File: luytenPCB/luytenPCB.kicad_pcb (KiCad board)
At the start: 2 copper layers, 35 parts, among them IC1 DRV8212DRLR, IC2 DRV8212DRLR, J1 Battery, J10 START_M, J2 BDC1, J3 BDC2, J4 LINE_RF, J5 LINE_LF, J6 DIST_L, J7 DIST_LM, J8 DIST_R, J9 DIST_RM, SW1 SW_SPST, SW2 ProgSelect

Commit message: pcb production prototype done
finished schematic and layout
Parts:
- added F1: 15A, Fuse:Fuse_1206_3216Metric_Pad1.42x1.75mm_HandSolder, F.Cu at (89.3, 46.2)
- added H1: MountingHole, MountingHole:MountingHole_2.2mm_M2_ISO7380, F.Cu at (44.3, 33.0)
- added H2: MountingHole, MountingHole:MountingHole_2.2mm_M2_ISO7380, F.Cu at (120.3, 33.0)
- added H3: MountingHole, MountingHole:MountingHole_2.2mm_M2_ISO7380, F.Cu at (44.3, 57.0)
- added H4: MountingHole, MountingHole:MountingHole_2.2mm_M2_ISO7380, F.Cu at (120.3, 57.0)
- J1: footprint Connector_AMASS:AMASS_XT30PW-M_1x02_P2.50mm_Horizontal -> Connector_AMASS:AMASS_XT30U-M_1x02_P5.0mm_Vertical
- moved C4 74.9 mm to (55.1, 41.5)
- moved C5 74.9 mm to (55.1, 44.5)
- moved C6 74.9 mm to (55.1, 47.5)
- moved C3 44.8 mm to (85.3, 41.7), turned to 180 degrees
- moved C2 43.4 mm to (85.3, 44.7), turned to 180 degrees
- moved C1 42.7 mm to (85.3, 47.7), turned to 180 degrees
- moved IC2 37.6 mm to (93.0, 37.9)
- moved C7 36.6 mm to (96.5, 38.2), turned to 90 degrees
- moved D3 32.4 mm to (81.2, 54.3)
- moved D4 26.2 mm to (71.1, 54.3)
- moved R1 26.1 mm to (103.5, 53.8), turned to 90 degrees
- moved R3 23.4 mm to (85.7, 54.0), turned to 180 degrees
- moved J1 22.8 mm to (114.9, 36.4)
- moved D1 21.0 mm to (103.5, 48.9), turned to -90 degrees
- moved R2 20.8 mm to (100.3, 53.8), turned to 90 degrees
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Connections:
- A1 pad D11: MDC2_2 -> MDC2_1
- A1 pad D12: MDC2_1 -> MDC2_2
- A1 pad D2: MDC1_2 -> MDC1_1
- A1 pad D3: MDC1_1 -> MDC1_2
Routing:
- net Arduino3.3V: track 0.00 -> 157.4 mm, vias 0 -> 3
- net START_SIGNAL: track 0.00 -> 67.7 mm, vias 0 -> 2
- net PS3: track 0.00 -> 53.1 mm, vias 0 -> 2
- net Net-(IC2-OUT1): track 0.00 -> 47.8 mm, vias 0 -> 2
- net DIST_L_INT: track 0.00 -> 47.4 mm, vias 0 -> 1
- net ArduinoVIN: track 0.00 -> 47.4 mm, vias 0 -> 4
- net PS2: track 0.00 -> 46.2 mm, vias 0 -> 2
- net Net-(IC2-OUT2): track 0.00 -> 44.8 mm, vias 0 -> 2
- net GND: track 0.00 -> 44.3 mm, vias 0 -> 8
- net MDC2_2: track 0.00 -> 43.4 mm, vias 0 -> 2
- net MDC2_1: track 0.00 -> 39.9 mm, vias 0 -> 2
- net PS1: track 0.00 -> 39.0 mm, vias 0 -> 2
- net Net-(IC1-OUT2): track 0.00 -> 32.3 mm, vias 0 -> 2
- net DIST_LM_INT: track 0.00 -> 31.7 mm
- net Net-(J1-Pin_1): track 0.00 -> 28.4 mm, vias 0 -> 2
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- added copper zone on B.Cu, net GND
- added copper zone on F.Cu, net GND
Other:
- board outline added: 80.9 x 35.6 mm
- board text added: "LUYTEN"
- board text added: "Luyten_MiniSumo_v0 - Alex Peng '24"

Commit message: updates
--fixes to routing, updated screw terminal
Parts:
- added D7: GREEN, Capacitor_SMD:C_0603_1608Metric_Pad1.08x0.95mm_HandSolder, F.Cu at (73.9, 55.6)
- added J11: DIST_C, Connector_PinHeader_2.54mm:PinHeader_1x03_P2.54mm_Vertical, F.Cu at (72.4, 58.8)
- added R7: 100, Diode_SMD:D_0805_2012Metric_Pad1.15x1.40mm_HandSolder, F.Cu at (74.0, 53.6)
- J2, J3: footprint Connector_Phoenix_MSTB:PhoenixContact_MSTBA_2,5_2-G_1x02_P5.00mm_Horizontal -> Connector_PinHeader_2.54mm:PinHeader_1x02_P2.54mm_Vertical
- J4, J5, J6, J7, J8, J9: footprint Connector_Phoenix_MSTB:PhoenixContact_MSTBA_2,5_3-G_1x03_P5.00mm_Horizontal -> Connector_PinHeader_2.54mm:PinHeader_1x03_P2.54mm_Vertical
- moved D3 16.7 mm to (97.6, 57.3)
- moved R3 16.7 mm to (102.1, 57.0)
- moved J4 14.7 mm to (58.8, 31.0), turned to 90 degrees
- moved D4 11.5 mm to (82.5, 54.9)
- moved R4 11.5 mm to (87.4, 54.7)
- moved J9 7.05 mm to (61.5, 58.7), turned to 90 degrees
- moved J6 6.50 mm to (97.8, 60.1), turned to 90 degrees
- moved J3 5.62 mm to (50.2, 31.0), turned to 90 degrees
- moved J5 4.54 mm to (105.7, 31.4), turned to -90 degrees
- moved D6 3.96 mm to (54.7, 55.4), turned to 180 degrees
- moved R5 3.79 mm to (62.1, 53.6)
- moved J7 1.64 mm to (85.2, 59.8), turned to 90 degrees
- moved D5 1.51 mm to (61.9, 55.6), turned to 180 degrees
- moved R6 1.18 mm to (54.5, 53.4)
- moved J2 1.01 mm to (114.9, 30.7), turned to -90 degrees
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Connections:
- A1 pad A4: unconnected-(A1-A4/SDA-PadA4) -> MDC2_1
- A1 pad A5: unconnected-(A1-A5/SCL-PadA5) -> MDC2_2
- A1 pad A6: unconnected-(A1-PadA6) -> MDC1_1
- A1 pad A7: unconnected-(A1-PadA7) -> MDC1_2
- A1 pad D11: MDC2_1 -> unconnected-(A1-D11_MOSI-PadD11)
- A1 pad D12: MDC2_2 -> unconnected-(A1-D12_MISO-PadD12)
- A1 pad D2: MDC1_1 -> unconnected-(A1-PadD2)
- A1 pad D3: MDC1_2 -> unconnected-(A1-PadD3)
- A1 pad D9: unconnected-(A1-PadD9) -> DIST_C_INT
- J1 pad 1: Net-(J1-Pin_1) -> GND
- J1 pad 2: GND -> Net-(J1-Pin_2)
- SW1 pad 2: Net-(J1-Pin_1) -> Net-(J1-Pin_2)
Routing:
- net Arduino3.3V: track 157.4 -> 27.8 mm, vias 3 -> 0
- net Net-(IC2-OUT1): track 47.8 -> 0.00 mm, vias 2 -> 0
- net DIST_L_INT: track 47.4 -> 0.00 mm, vias 1 -> 0
- net Net-(IC2-OUT2): track 44.8 -> 0.00 mm, vias 2 -> 0
- net Net-(IC1-OUT2): track 32.3 -> 0.00 mm, vias 2 -> 0
- net DIST_LM_INT: track 31.7 -> 0.00 mm
- net Net-(J1-Pin_1): track 28.4 -> 0.00 mm, vias 2 -> 0
- net LF_INT: track 27.7 -> 0.00 mm
- net Net-(IC1-OUT1): track 25.6 -> 0.00 mm, vias 2 -> 0
- net Net-(J1-Pin_2): track 0.00 -> 23.8 mm, vias 0 -> 2
- net DIST_RM_INT: track 18.4 -> 0.00 mm
- net MDC2_2: track 43.4 -> 27.8 mm, vias 2 -> 0
- net RF_INT: track 14.3 -> 0.00 mm
- net DIST_R_INT: track 9.76 -> 0.00 mm
- net MDC2_1: track 39.9 -> 30.4 mm, vias 2 -> 0
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- removed copper zone on B.Cu, net GND
- removed copper zone on F.Cu, net GND

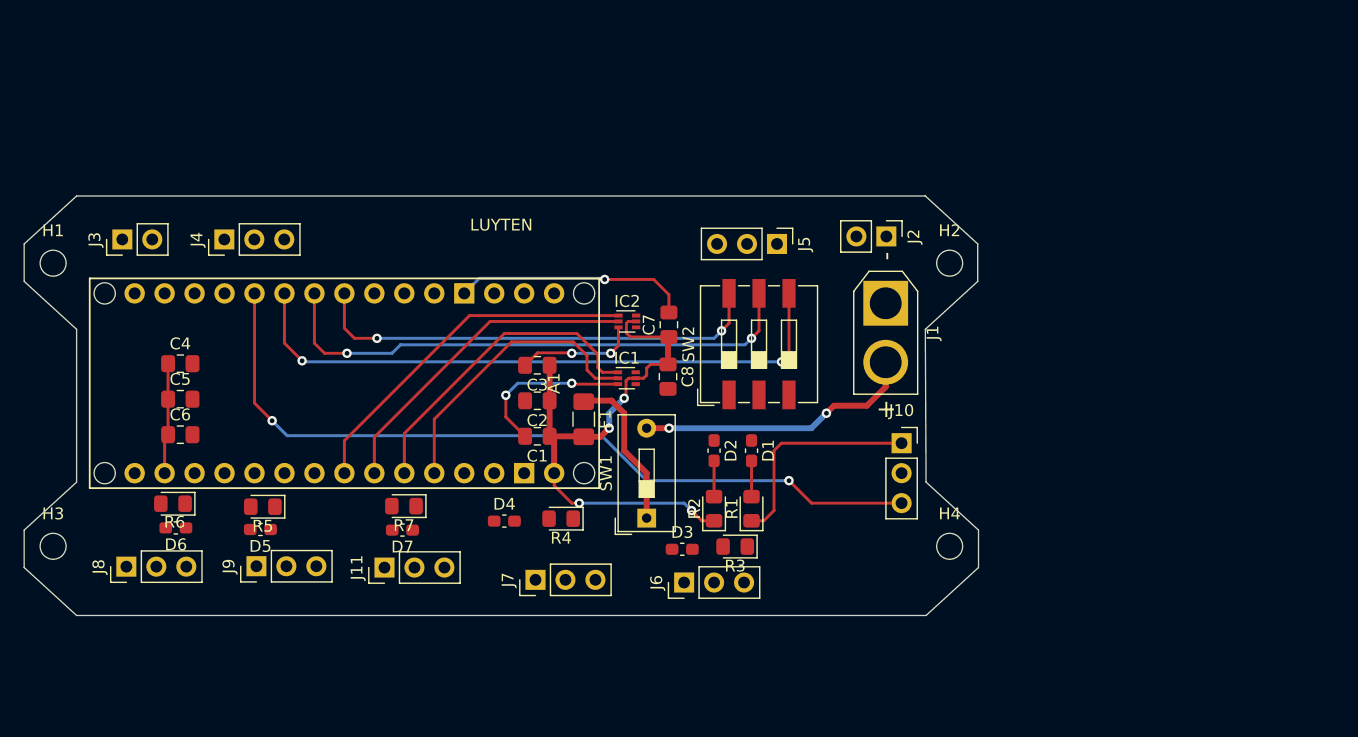
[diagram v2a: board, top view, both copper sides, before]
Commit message: luytenv2
forgot to update spst footprint :(
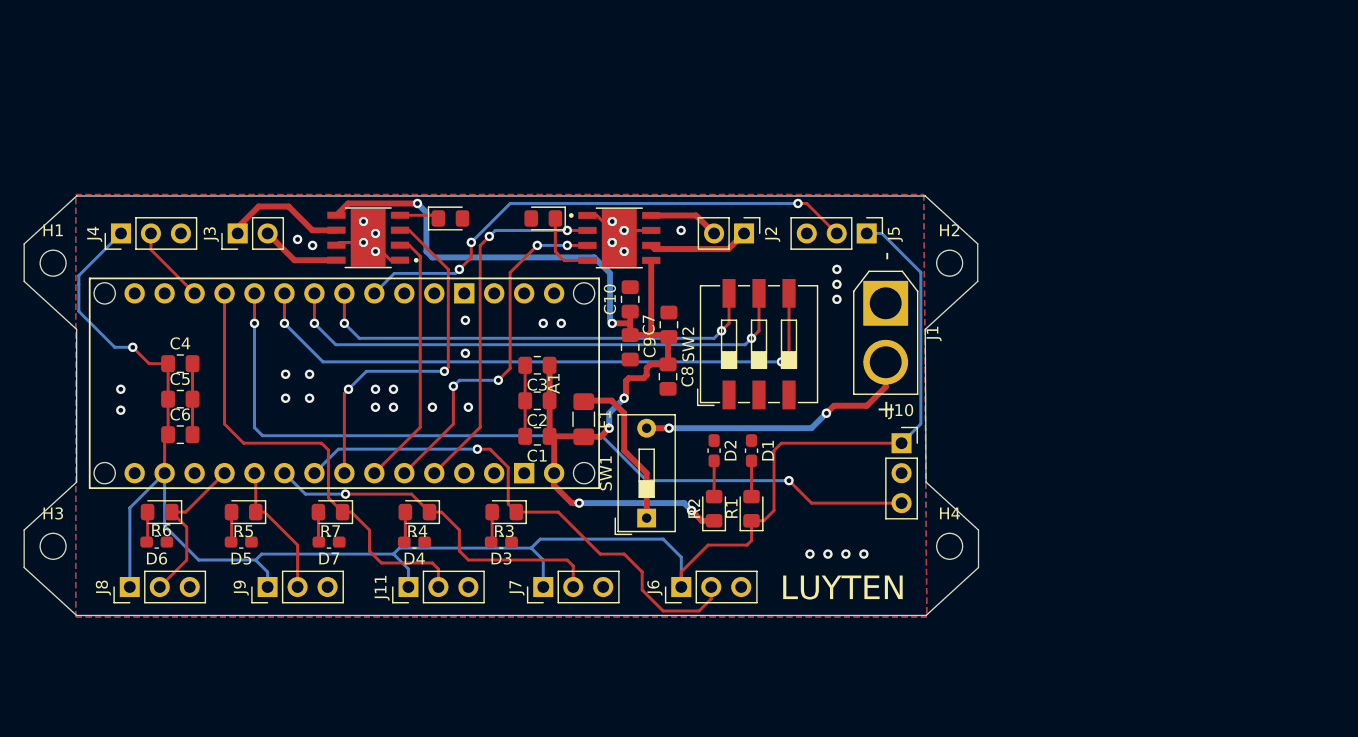
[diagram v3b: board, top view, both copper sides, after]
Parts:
- added C10: 47uF, Capacitor_SMD:C_0805_2012Metric_Pad1.18x1.45mm_HandSolder, F.Cu at (93.2, 36.1)
- added C9: 47uF, Capacitor_SMD:C_0805_2012Metric_Pad1.18x1.45mm_HandSolder, F.Cu at (93.2, 40.1)
- added R8: 30k, Diode_SMD:D_0805_2012Metric_Pad1.15x1.40mm_HandSolder, F.Cu at (85.9, 29.2)
- added R9: 30k, Diode_SMD:D_0805_2012Metric_Pad1.15x1.40mm_HandSolder, F.Cu at (78.0, 29.2)
- IC1, IC2: footprint Package_TO_SOT_SMD:SOT-563 -> DRV8871DDAR:VREG_LM5017MR_NOPB
- moved IC2 23.1 mm to (71.0, 30.8), turned to 180 degrees
- moved R3 19.8 mm to (82.5, 54.1)
- moved D3 15.3 mm to (82.3, 56.6), turned to 180 degrees
- moved R4 12.2 mm to (75.2, 54.1)
- moved J2 12.1 mm to (102.9, 30.5)
- moved IC1 11.9 mm to (92.3, 30.9)
- moved J3 9.79 mm to (59.9, 30.5)
- moved J4 8.78 mm to (50.1, 30.5)
- moved D4 7.82 mm to (74.9, 56.6), turned to 180 degrees
- moved J5 7.66 mm to (113.3, 30.5)
- moved D7 6.31 mm to (67.7, 56.6)
- moved R7 6.24 mm to (67.8, 54.1)
- moved J11 2.62 mm to (74.4, 60.5)
- moved D6 2.02 mm to (53.1, 56.6)
- moved J9 2.00 mm to (62.5, 60.5)
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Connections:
- IC1 pad 1: MDC1_1 -> GND
- IC1 pad 3: GND -> MDC1_1
- IC1 pad 4: Net-(IC1-OUT2) -> Net-(IC1-ILIM)
- IC2 pad 1: MDC2_1 -> GND
- IC2 pad 3: GND -> MDC2_1
- IC2 pad 4: Net-(IC2-OUT2) -> Net-(IC2-ILIM)
- J2 pad 1: Net-(IC1-OUT2) -> Net-(IC1-OUT1)
- J2 pad 2: Net-(IC1-OUT1) -> Net-(IC1-OUT2)
- J3 pad 1: Net-(IC2-OUT2) -> Net-(IC2-OUT1)
- J3 pad 2: Net-(IC2-OUT1) -> Net-(IC2-OUT2)
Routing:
- net Arduino3.3V: track 27.8 -> 150.4 mm, vias 0 -> 1
- net DIST_L_INT: track 0.00 -> 44.3 mm, vias 0 -> 1
- net LF_INT: track 0.00 -> 44.2 mm, vias 0 -> 3
- net ArduinoVIN: track 47.4 -> 87.5 mm, vias 4 -> 6
- net DIST_C_INT: track 0.00 -> 39.2 mm
- net DIST_LM_INT: track 0.00 -> 30.6 mm, vias 0 -> 1
- net GND: track 44.3 -> 24.4 mm, vias 5 -> 34
- net DIST_R_INT: track 0.00 -> 13.7 mm
- net DIST_RM_INT: track 0.00 -> 11.6 mm
- net Net-(IC2-OUT1): track 0.00 -> 10.4 mm
- net Net-(IC1-OUT1): track 0.00 -> 8.54 mm
- net Net-(IC2-OUT2): track 0.00 -> 6.76 mm
- net RF_INT: track 0.00 -> 6.61 mm
- net Net-(IC1-OUT2): track 0.00 -> 5.97 mm
- net Net-(IC1-ILIM): track 0.00 -> 5.83 mm
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- added copper zone on B.Cu, net GND
- added copper zone on F.Cu, net GND
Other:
- board text added: "Luyten_MiniSumo_v1 - Alex Peng '24"
- board text removed: "Luyten_MiniSumo_v0 - Alex Peng '24"

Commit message: revision
changed from nano esp32 -> nano every, added dummy connection for optional kill switch circuitry, fixed switch footprint, removed leds from analog sensors
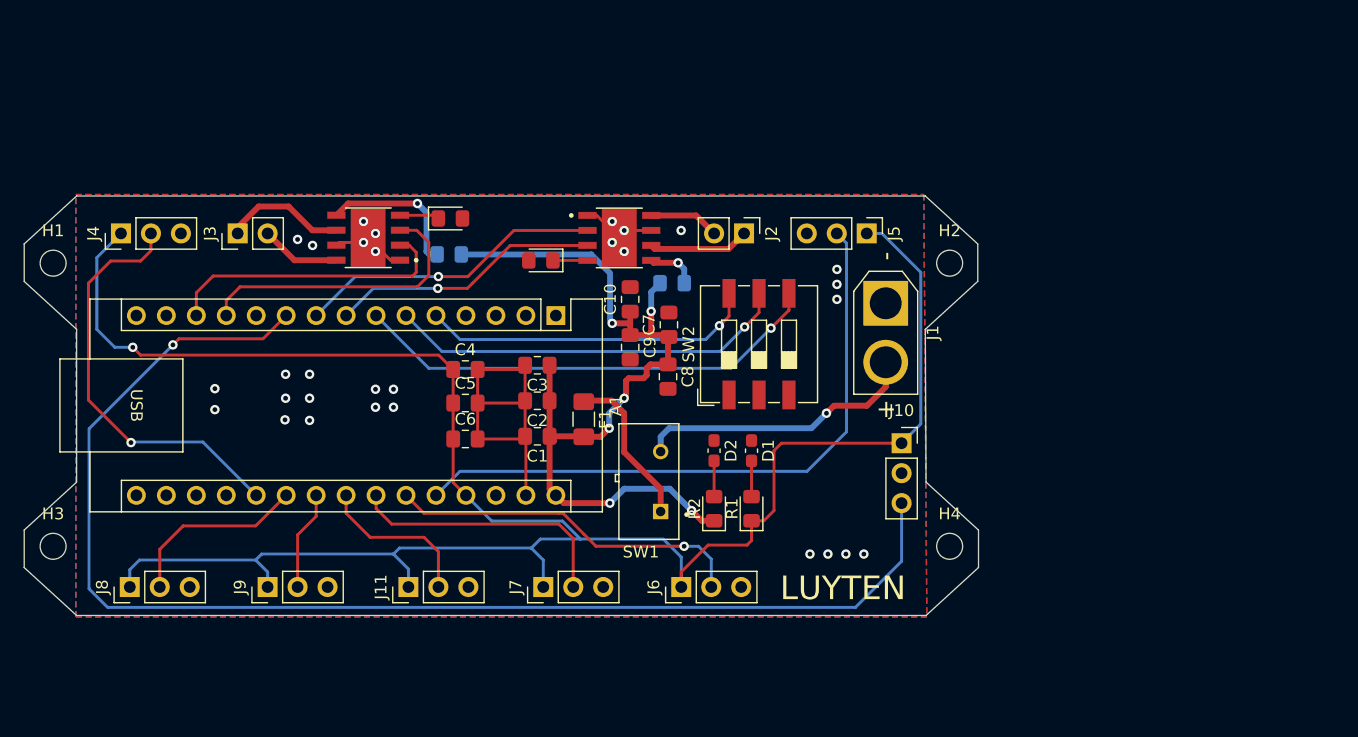
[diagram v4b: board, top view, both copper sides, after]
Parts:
- removed D3, D4, D5, D6, D7: GREEN, Capacitor_SMD:C_0603_1608Metric_Pad1.08x0.95mm_HandSolder
- removed R5, R6, R7: 100, Diode_SMD:D_0805_2012Metric_Pad1.15x1.40mm_HandSolder
- A1: footprint PCM_arduino-library:Arduino_Nano_ESP32_Socket -> Module:Arduino_Nano
- R1: value 100 -> 600
- R3, R4: value 100 -> 600; moved to B.Cu
- SW1: footprint Button_Switch_THT:SW_DIP_SPSTx01_Slide_9.78x4.72mm_W7.62mm_P2.54mm -> Button_Switch_THT:SW_AS11CP
- moved A1 39.9 mm to (86.9, 37.4)
- moved C4 24.2 mm to (79.2, 42.0)
- moved C6 24.2 mm to (79.2, 47.9)
- moved C5 24.2 mm to (79.2, 44.9)
- moved R3 24.1 mm to (96.8, 34.7), turned to 0 degrees
- moved R4 22.0 mm to (77.9, 32.3)
- moved R8 3.56 mm to (85.6, 32.8)
- moved SW1 3.10 mm to (94.8, 51.5), turned to 180 degrees
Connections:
- C4 pad 1: Arduino3.3V -> Arduino5V
- C5 pad 1: Arduino3.3V -> Arduino5V
- C6 pad 1: Arduino3.3V -> Arduino5V
- IC1 pad 5: ArduinoVIN -> Net-(IC1-VM)
- IC2 pad 5: ArduinoVIN -> Net-(IC2-VM)
- J10 pad 1: Arduino3.3V -> Arduino5V
- J11 pad 1: Arduino3.3V -> Arduino5V
- J4 pad 1: Arduino3.3V -> Arduino5V
- J5 pad 1: Arduino3.3V -> Arduino5V
- J6 pad 1: Arduino3.3V -> Arduino5V
- J7 pad 1: Arduino3.3V -> Arduino5V
- J8 pad 1: Arduino3.3V -> Arduino5V
- J9 pad 1: Arduino3.3V -> Arduino5V
- R1 pad 1: Arduino3.3V -> Arduino5V
- R3 pad 1: DIST_L_INT -> ArduinoVIN
- R3 pad 2: Net-(D3-A) -> Net-(IC1-VM)
- R4 pad 1: DIST_LM_INT -> ArduinoVIN
- R4 pad 2: Net-(D4-A) -> Net-(IC2-VM)
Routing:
- net Arduino5V: track 0.00 -> 174.7 mm, vias 0 -> 1
- net Arduino3.3V: track 150.4 -> 0.00 mm, vias 1 -> 0
- net START_SIGNAL: track 68.9 -> 110.3 mm, vias 2 -> 1
- net RF_INT: track 6.61 -> 35.4 mm, vias 0 -> 1
- net DIST_C_INT: track 39.2 -> 13.7 mm
- net GND: track 24.4 -> 41.7 mm, vias 34 -> 30
- net ArduinoVIN: track 87.5 -> 73.1 mm
- net DIST_L_INT: track 44.3 -> 30.5 mm
- net Net-(IC2-VM): track 0.00 -> 12.7 mm, vias 0 -> 1
- net PS3: track 52.1 -> 40.3 mm, vias 2 -> 1
- net PS2: track 44.6 -> 34.2 mm, vias 2 -> 1
- net PS1: track 38.7 -> 28.4 mm, vias 2 -> 1
- net LF_INT: track 44.2 -> 54.2 mm, vias 3 -> 0
- net DIST_LM_INT: track 30.6 -> 23.0 mm, vias 1 -> 0
- net MDC1_1: track 30.2 -> 22.9 mm, vias 4 -> 1
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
